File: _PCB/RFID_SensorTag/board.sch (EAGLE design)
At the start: 7 parts, among them M2 BATTERY-CHARGER-LI-PROT, X1 53048-02

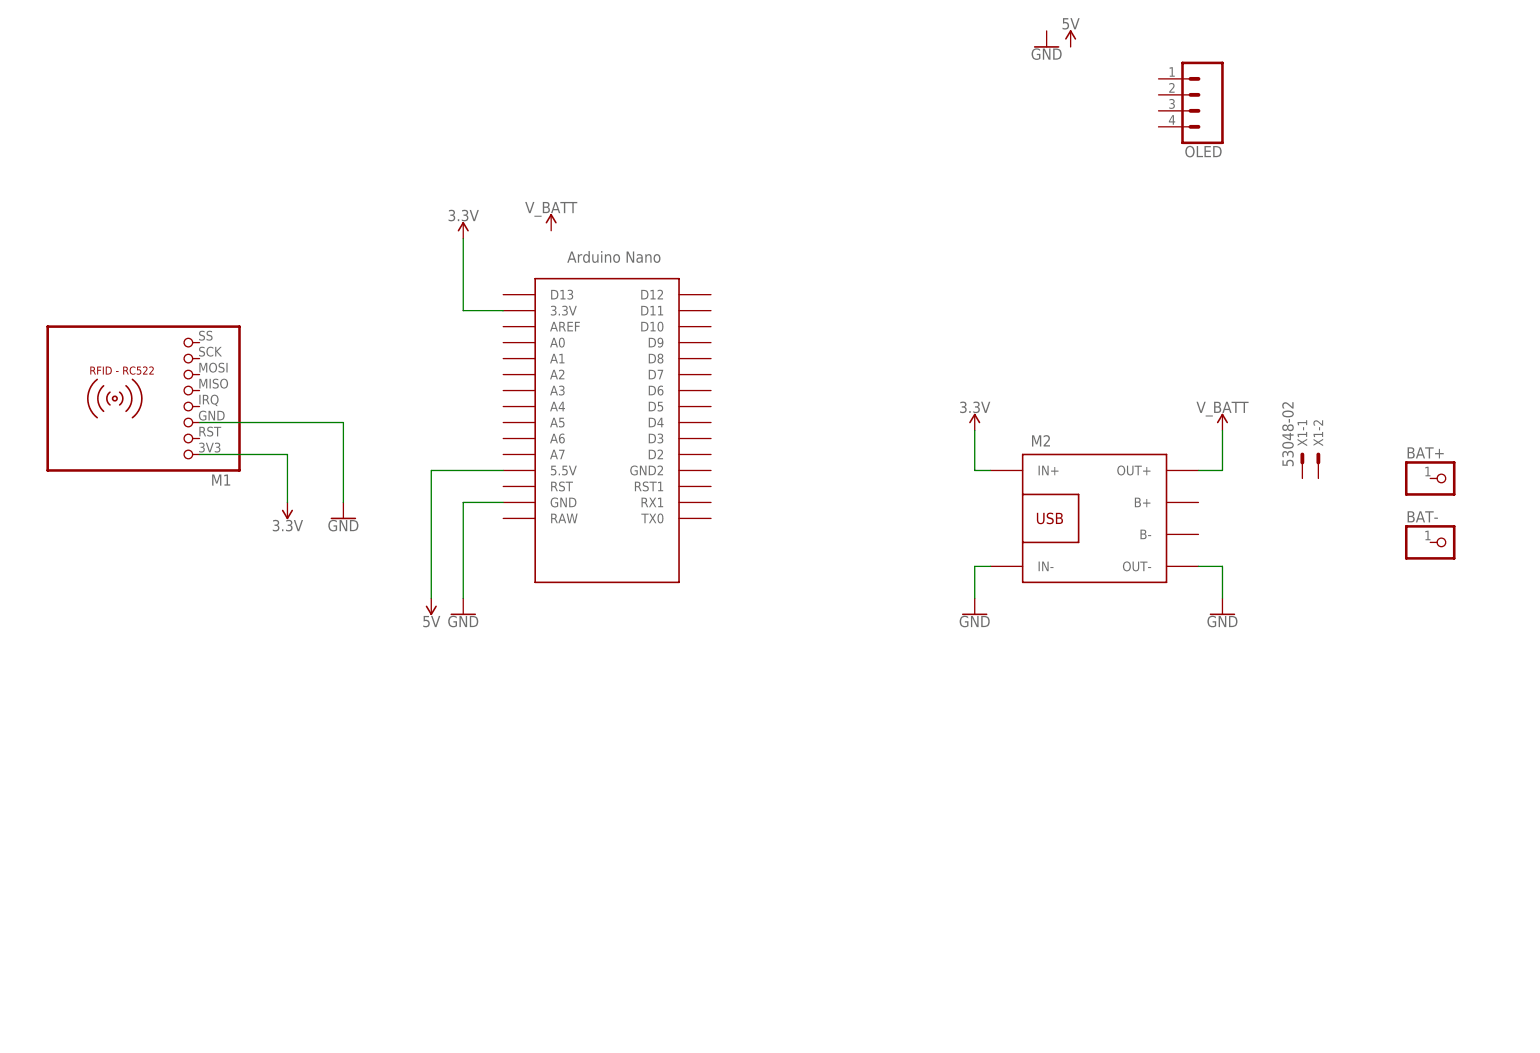
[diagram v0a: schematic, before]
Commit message: PCB - RFID system update
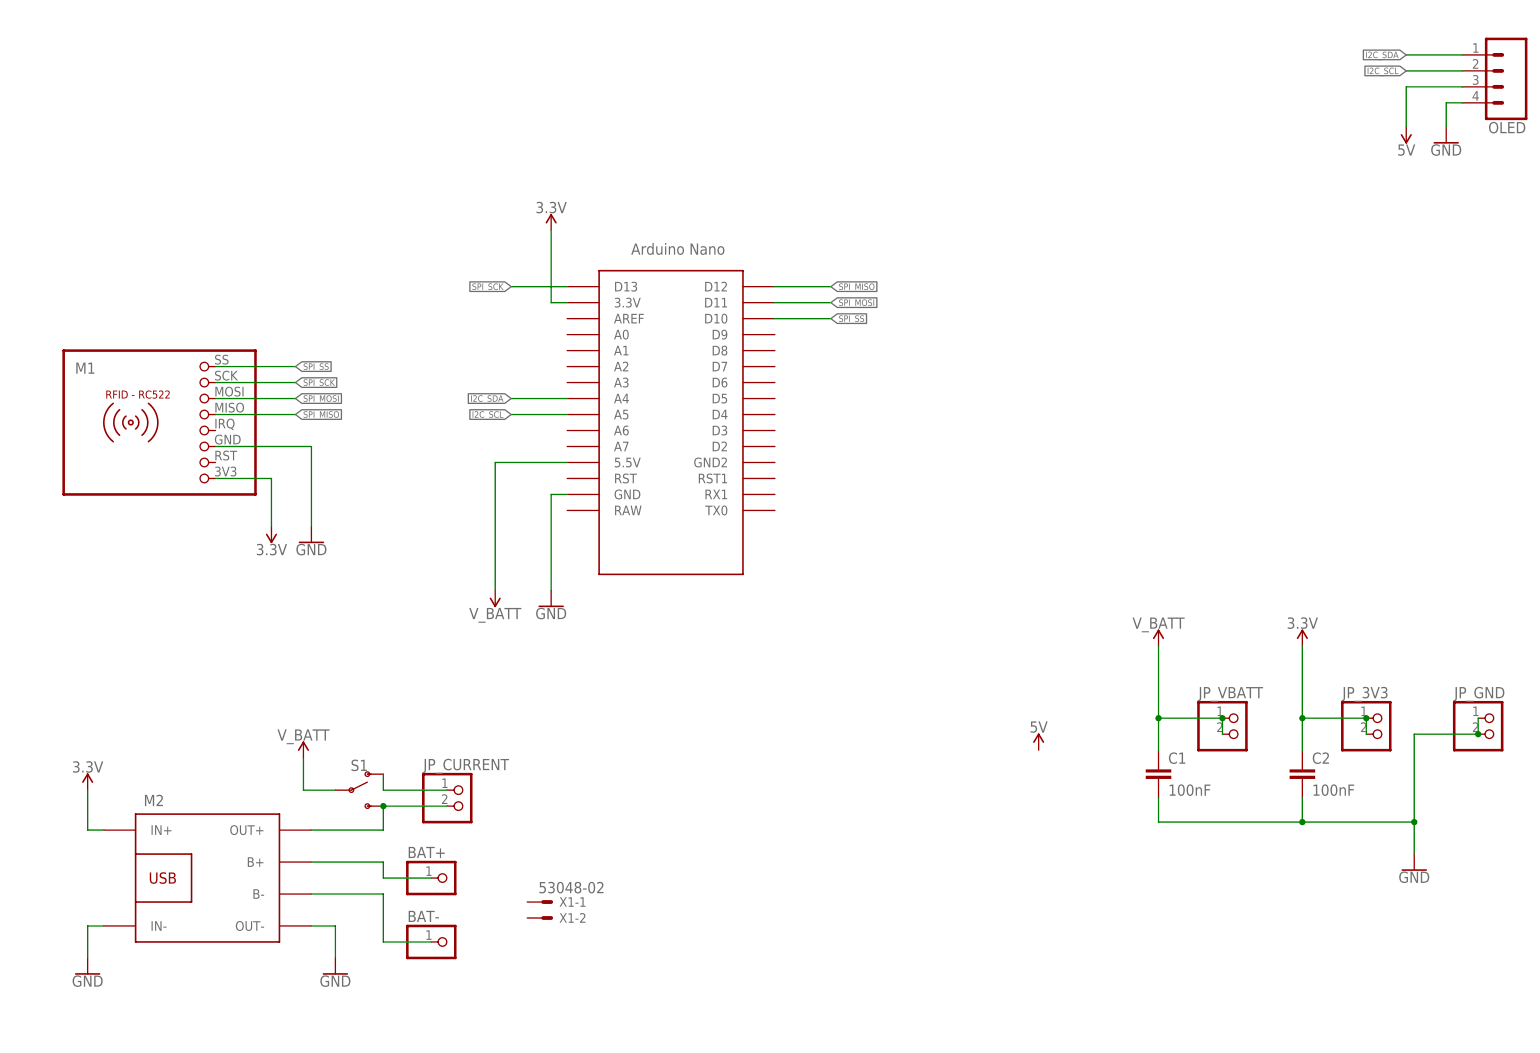
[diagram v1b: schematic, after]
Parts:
- added C1, C2: 100nF, rcl:C-EUC0805
- added JP_3V3, JP_CURRENT, JP_GND, JP_VBATT: (no value), pinhead:PINHD-1X2
- added S1: (no value), SparkFun-Switches:SWITCH-SPDT-PTH-11.6X4.0MM
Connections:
- new net I2C_SCL: OLED.2, U$1.A5
- new net I2C_SDA: OLED.1, U$1.A4
- new net N$1: JP_CURRENT.2, M2.OUT+, S1.S
- new net N$2: JP_CURRENT.1, S1.O
- new net N$3: BAT+.1, M2.B+
- new net N$4: BAT-.1, M2.B-
- new net SPI_MISO: M1.5, U$1.D12
- new net SPI_MOSI: M1.6, U$1.D11
- new net SPI_SCK: M1.7, U$1.D13
- new net SPI_SS: M1.8, U$1.D10
- net 3.3V: now also C2.1, JP_3V3.1, JP_3V3.2
- net 5V: now also OLED.3; no longer U$1.5.5V
- net GND: now also C1.2, C2.2, JP_GND.1, JP_GND.2, OLED.4
- net V_BATT: now also C1.1, JP_VBATT.1, JP_VBATT.2, S1.P, U$1.5.5V; no longer M2.OUT+
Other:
- moved on the sheet: BAT+, BAT-, M1, M2, OLED, X1-1, X1-2

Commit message: PCB schematic update
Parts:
- removed OLED: (no value), SparkFun-Connectors:CONN_04
- added OLED_1, OLED_2: (no value), SparkFun-Connectors:CONN_04
- renumbered JP_CURRENT to CURRENT
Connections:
- removed net N$3: BAT+.1, M2.B+
- removed net N$4: BAT-.1, M2.B-
- new net BATT+: BAT+.1, M2.B+, X1-1.S
- new net BATT-: BAT-.1, M2.B-, X1-2.S
- net 5V: now also OLED_1.3, OLED_2.4; no longer OLED.3
- net GND: now also OLED_1.4, OLED_2.3; no longer OLED.4
- net I2C_SCL: now also OLED_1.2, OLED_2.2; no longer OLED.2
- net I2C_SDA: now also OLED_1.1, OLED_2.1; no longer OLED.1

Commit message: PCB ver1
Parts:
- removed BAT+, BAT-: (no value), pinhead_v2:PINHD-1X1/LONG
- added C3: 100nF, rcl:C-EUC0805
- added JP_BATT: (no value), pinhead:PINHD-1X2
- added JP_BATT_EN: JUMPER-SMT_2_NC_PASTE_SILK, SparkFun-Jumpers:JUMPER-SMT_2_NC_PASTE_SILK
- added U1: MAXIM_ELECTRONICS_MAX40200AUK+MAXIM_ELECTRONICS_MAX40200AUK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, Maxim Electronics - MAX40200AUK+:MAXIM_ELECTRONICS_MAX40200AUK+MAXIM_ELECTRONICS_MAX40200AUK+_0_0
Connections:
- removed net 5V: OLED_1.3, OLED_2.4
- removed net BATT+: BAT+.1, M2.B+, X1-1.S
- removed net BATT-: BAT-.1, M2.B-, X1-2.S
- removed net N$1: CURRENT.2, M2.OUT+, S1.S
- new net BATT_VOUT: S1.P, U1.EN, U1.VDD
- new net N$3: JP_BATT.1, JP_BATT_EN.2, X1-1.S
- new net N$4: CURRENT.2, S1.S
- new net N$5: JP_BATT.2, M2.B-, X1-2.S
- new net N$6: JP_BATT_EN.1, M2.B+
- net 3.3V: now also OLED_1.3, OLED_2.4; no longer M2.IN+
- net GND: now also C3.2, U1.GND, U1.NC
- net N$2: now also M2.OUT+
- net V_BATT: now also C3.1, U1.OUT; no longer S1.P
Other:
- moved on the sheet: CURRENT, M1, M2, S1, X1-1, X1-2

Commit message: RFID PCB v2
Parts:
- removed C3: 100nF, rcl:C-EUC0805
- removed JP_BATT, JP_VBATT: (no value), pinhead:PINHD-1X2
- added BATT, JP_VBATT/5V: (no value), pinhead:PINHD-1X2
- added C4: 100nF, rcl:C-EUC0805
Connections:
- new net BUZZER: U$1.D8
- new net RFID_RST: M1.2, U$1.D9
- net 3.3V: now also C1.1; no longer C2.1
- net GND: now also C4.2; no longer C3.2
- net N$3: now also BATT.1; no longer JP_BATT.1
- net N$5: now also BATT.2; no longer JP_BATT.2
- net V_BATT: now also C2.1, C4.1, JP_VBATT/5V.1, JP_VBATT/5V.2; no longer C1.1, C3.1, JP_VBATT.1, JP_VBATT.2
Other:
- moved on the sheet: C1, C2, JP_3V3, JP_GND
